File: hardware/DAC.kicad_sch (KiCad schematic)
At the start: 43 parts, among them J2 PJ-3270, U10 OPA1652, U11 LM4562, U9 WM8741

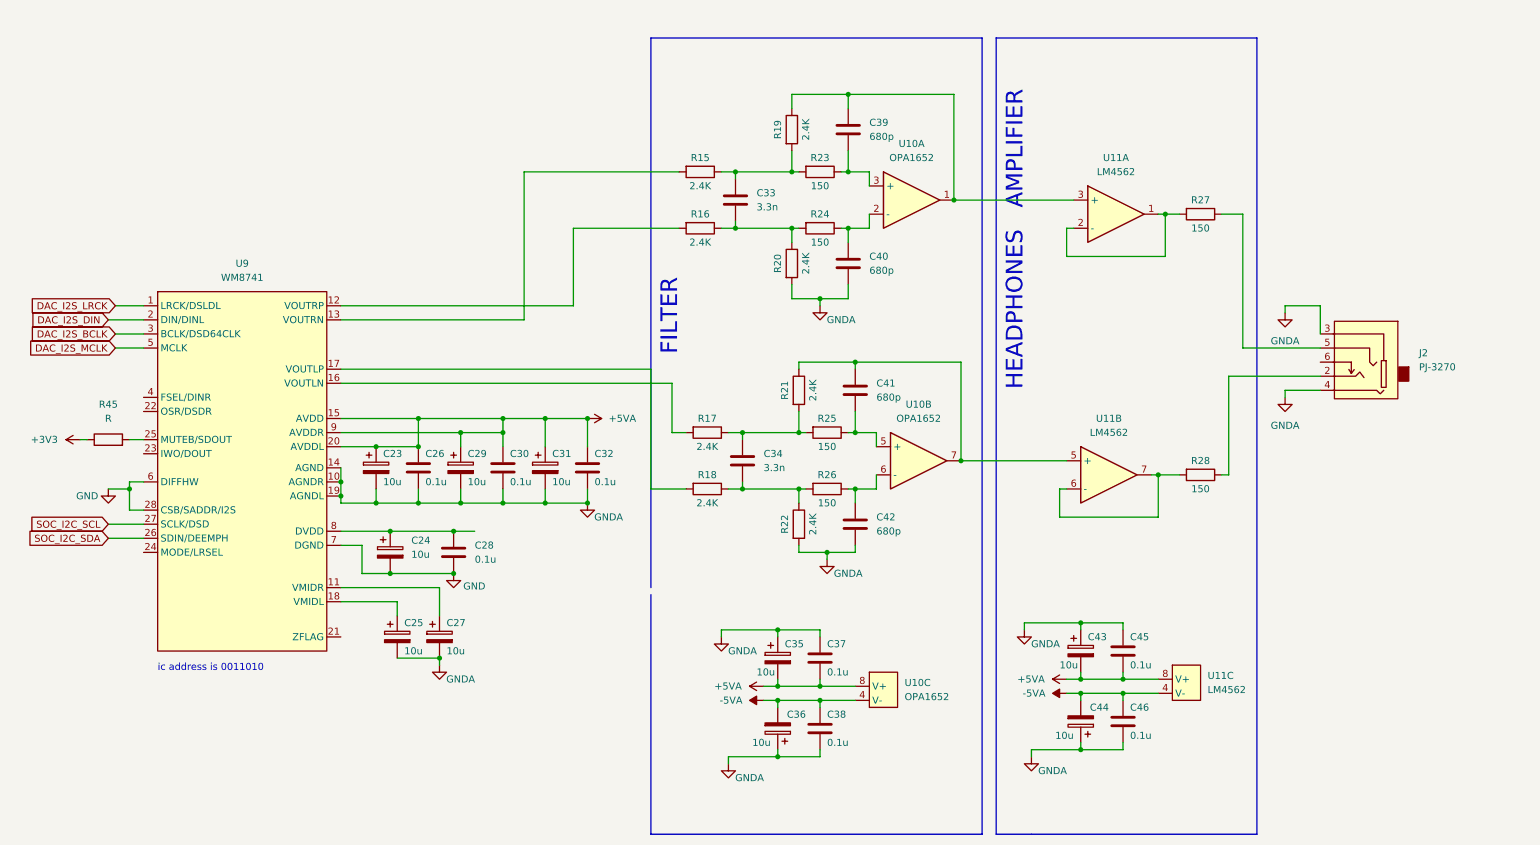
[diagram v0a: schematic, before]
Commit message: added hierarchy labels
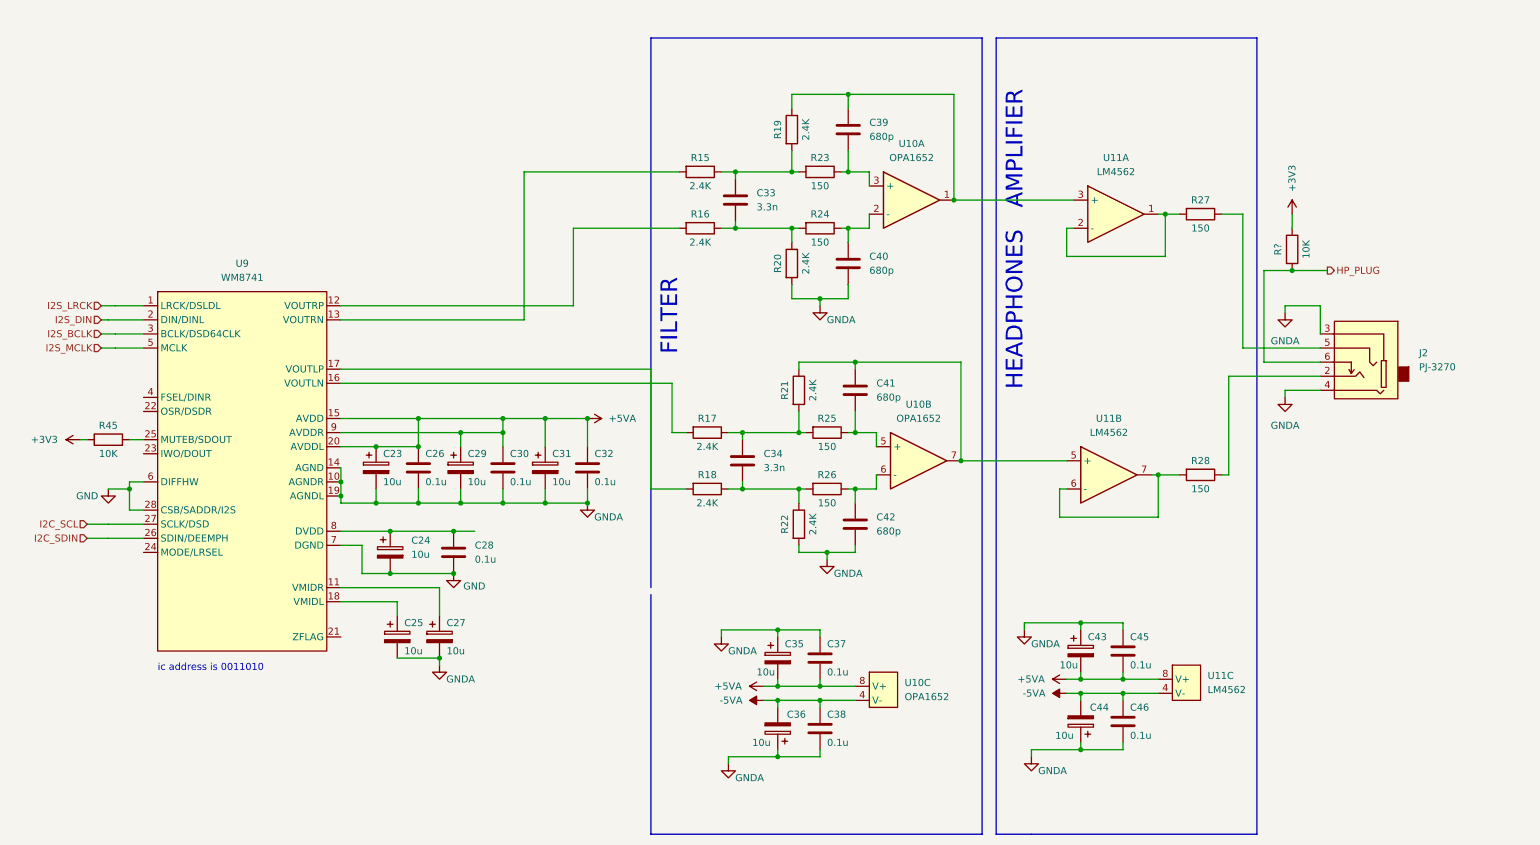
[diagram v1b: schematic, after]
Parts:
- added R?: 10K, symbol rlib_passive:R
- R45: value R -> 10K
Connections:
- net +3V3: now also R?.1
- net HP_PLUG: now reaches J2.6
- net HP_PLUG: now also R?.2
- net DAC_I2S_BCLK renamed I2S_BCLK
- net DAC_I2S_DIN renamed I2S_DIN
- net DAC_I2S_LRCK renamed I2S_LRCK
- net DAC_I2S_MCLK renamed I2S_MCLK
- net SOC_I2C_SCL renamed I2C_SCL
- net SOC_I2C_SDA renamed I2C_SDIN
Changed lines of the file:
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@@
   (junction (at 204.47 120.65) (diameter 0) (color 0 0 0 1)
   )
+  (junction (at 242.57 57.15) (diameter 0) (color 0 0 0 0)
+  )
   (junction (at 152.4 49.53) (diameter 0) (color 0 0 0 1)
   )
@@
     (stroke (width 0) (type default) (color 0 0 0 1))
   )
+  (wire (pts (xy 25.4 102.87) (xy 29.21 102.87))
+    (stroke (width 0) (type default) (color 0 0 0 0))
+  )
   (wire (pts (xy 163.83 96.52) (xy 167.64 96.52))
     (stroke (width 0) (type default) (color 0 0 0 1))
@@
     (stroke (width 0) (type default) (color 0 0 0 1))
   )
+  (wire (pts (xy 27.94 66.04) (xy 29.21 66.04))
+    (stroke (width 0) (type default) (color 0 0 0 0))
+  )
   (polyline (pts (xy 127 115.57) (xy 127 158.75))
     (stroke (width 0) (type default) (color 0 0 0 0))
@@
     (stroke (width 0) (type default) (color 0 0 0 1))
   )
+  (wire (pts (xy 242.57 57.15) (xy 248.92 57.15))
+    (stroke (width 0) (type default) (color 0 0 0 0))
+  )
   (wire (pts (xy 158.75 107.95) (xy 158.75 109.22))
     (stroke (width 0) (type default) (color 0 0 0 1))
@@
     (stroke (width 0) (type default) (color 0 0 0 1))
   )
+  (wire (pts (xy 247.65 73.66) (xy 237.49 73.66))
+    (stroke (width 0) (type default) (color 0 0 0 0))
+  )
   (wire (pts (xy 229.87 93.98) (xy 231.14 93.98))
     (stroke (width 0) (type default) (color 0 0 0 1))
@@
     (stroke (width 0) (type default) (color 0 0 0 1))
   )
+  (wire (pts (xy 242.57 57.15) (xy 237.49 57.15))
+    (stroke (width 0) (type default) (color 0 0 0 0))
+  )
   (wire (pts (xy 204.47 143.51) (xy 204.47 142.24))
     (stroke (width 0) (type default) (color 0 0 0 1))
@@
     (stroke (width 0) (type default) (color 0 0 0 1))
   )
+  (wire (pts (xy 27.94 71.12) (xy 30.48 71.12))
+    (stroke (width 0) (type default) (color 0 0 0 0))
+  )
   (wire (pts (xy 218.44 93.98) (xy 222.25 93.98))
     (stroke (width 0) (type default) (color 0 0 0 1))
@@
     (stroke (width 0) (type default) (color 0 0 0 1))
   )
+  (wire (pts (xy 27.94 63.5) (xy 30.48 63.5))
+    (stroke (width 0) (type default) (color 0 0 0 0))
+  )
+  (wire (pts (xy 237.49 73.66) (xy 237.49 57.15))
+    (stroke (width 0) (type default) (color 0 0 0 0))
+  )
   (wire (pts (xy 231.14 93.98) (xy 231.14 76.2))
     (stroke (width 0) (type default) (color 0 0 0 1))
@@
     (stroke (width 0) (type default) (color 0 0 0 1))
   )
+  (wire (pts (xy 242.57 46.99) (xy 242.57 49.53))
+    (stroke (width 0) (type default) (color 0 0 0 0))
+  )
   (wire (pts (xy 229.87 46.99) (xy 233.68 46.99))
     (stroke (width 0) (type default) (color 0 0 0 1))
@@
   (wire (pts (xy 201.93 130.81) (xy 204.47 130.81))
     (stroke (width 0) (type default) (color 0 0 0 1))
+  )
+  (wire (pts (xy 25.4 105.41) (xy 29.21 105.41))
+    (stroke (width 0) (type default) (color 0 0 0 0))
+  )
+  (wire (pts (xy 27.94 68.58) (xy 30.48 68.58))
+    (stroke (width 0) (type default) (color 0 0 0 0))
   )
   (wire (pts (xy 219.71 46.99) (xy 218.44 46.99))
@@
     (effects (font (size 3 3)) (justify left bottom))
   )
-  (global_label "DAC_I2S_LRCK" (shape input) (at 30.48 63.5 180) (fields_autoplaced)
+  (hierarchical_label "I2S_LRCK" (shape input) (at 27.94 63.5 180)
     (effects (font (size 1.27 1.27)) (justify right))
-    (property "Intersheet References" "${INTERSHEET_REFS}" (id 0) (at 14.6412 63.4206 0)
-      (effects (font (size 1.27 1.27)) (justify right) hide)
-    )
-  )
-  (global_label "SOC_I2C_SDA" (shape input) (at 29.21 105.41 180) (fields_autoplaced)
+  )
+  (hierarchical_label "I2S_BCLK" (shape input) (at 27.94 68.58 180)
     (effects (font (size 1.27 1.27)) (justify right))
-    (property "Intersheet References" "${INTERSHEET_REFS}" (id 0) (at 14.3993 105.3306 0)
-      (effects (font (size 1.27 1.27)) (justify right) hide)
-    )
-  )
-  (global_label "DAC_I2S_DIN" (shape input) (at 29.21 66.04 180) (fields_autoplaced)
+  )
+  (hierarchical_label "I2S_MCLK" (shape input) (at 27.94 71.12 180)
     (effects (font (size 1.27 1.27)) (justify right))
-    (property "Intersheet References" "${INTERSHEET_REFS}" (id 0) (at 15.004 65.9606 0)
-      (effects (font (size 1.27 1.27)) (justify right) hide)
-    )
-  )
-  (global_label "DAC_I2S_MCLK" (shape input) (at 30.48 71.12 180) (fields_autoplaced)
+  )
+  (hierarchical_label "I2C_SCL" (shape input) (at 25.4 102.87 180)
     (effects (font (size 1.27 1.27)) (justify right))
-    (property "Intersheet References" "${INTERSHEET_REFS}" (id 0) (at 14.4598 71.0406 0)
-      (effects (font (size 1.27 1.27)) (justify right) hide)
-    )
-  )
-  (global_label "DAC_I2S_BCLK" (shape input) (at 30.48 68.58 180) (fields_autoplaced)
+  )
+  (hierarchical_label "I2S_DIN" (shape input) (at 27.94 66.04 180)
     (effects (font (size 1.27 1.27)) (justify right))
-    (property "Intersheet References" "${INTERSHEET_REFS}" (id 0) (at 14.6412 68.5006 0)
-      (effects (font (size 1.27 1.27)) (justify right) hide)
-    )
-  )
-  (global_label "SOC_I2C_SCL" (shape input) (at 29.21 102.87 180) (fields_autoplaced)
+  )
+  (hierarchical_label "I2C_SDIN" (shape input) (at 25.4 105.41 180)
     (effects (font (size 1.27 1.27)) (justify right))
-    (property "Intersheet References" "${INTERSHEET_REFS}" (id 0) (at 14.4598 102.7906 0)
-      (effects (font (size 1.27 1.27)) (justify right) hide)
-    )
+  )
+  (hierarchical_label "HP_PLUG" (shape output) (at 248.92 57.15 0)
+    (effects (font (size 1.27 1.27)) (justify left))
   )
   (symbol (lib_id "rlib_passive:C_Pol") (at 77.47 92.71 0) (unit 1)
@@
     (pin "1")
     (pin "2")
+  )
+  (symbol (lib_id "power:+3V3") (at 242.57 46.99 0) (unit 1)
+    (in_bom yes) (on_board yes)
+    (property "Reference" "#PWR?" (id 0) (at 242.57 50.8 0)
+      (effects (font (size 1.27 1.27)) hide)
+    )
+    (property "Value" "+3V3" (id 1) (at 242.57 38.1 90)
+      (effects (font (size 1.27 1.27)) (justify right))
+    )
+    (property "Footprint" "" (id 2) (at 242.57 46.99 0)
+      (effects (font (size 1.27 1.27)) hide)
+    )
+    (property "Datasheet" "" (id 3) (at 242.57 46.99 0)
+      (effects (font (size 1.27 1.27)) hide)
+    )
+    (pin "1")
   )
   (symbol (lib_id "rlib_passive:R") (at 137.16 86.36 270) (unit 1)
@@
   )
   (symbol (lib_id "rlib_passive:R") (at 29.21 87.63 90) (unit 1)
-    (in_bom yes) (on_board yes) (fields_autoplaced)
-    (property "Reference" "R45" (id 0) (at 29.21 81.28 90))
-    (property "Value" "R" (id 1) (at 29.21 83.82 90))
+    (in_bom yes) (on_board yes)
+    (property "Reference" "R45" (id 0) (at 29.21 85.09 90))
+    (property "Value" "10K" (id 1) (at 29.21 90.17 90))
     (property "Footprint" "rlib_passive:R_0603_1608Metric" (id 2) (at 29.21 89.408 90)
       (effects (font (size 1.27 1.27)) hide)
@@
     (pin "1")
     (pin "2")
+  )
+  (symbol (lib_id "rlib_passive:R") (at 242.57 53.34 0) (unit 1)
+    (in_bom yes) (on_board yes)
+    (property "Reference" "R?" (id 0) (at 240.03 53.34 90))
+    (property "Value" "10K" (id 1) (at 245.11 53.34 90))
+    (property "Footprint" "" (id 2) (at 240.792 53.34 90)
+      (effects (font (size 1.27 1.27)) hide)
+    )
+    (property "Datasheet" "~" (id 3) (at 242.57 53.34 0)
+      (effects (font (size 1.27 1.27)) hide)
+    )
+    (property "Tolerance" "" (id 4) (at 242.57 53.34 0))
+    (property "LSCS Partnumber" "" (id 5) (at 242.57 53.34 0))
+    (property "Manufacturer" "" (id 6) (at 242.57 53.34 0))
+    (pin "1")
+    (pin "2")

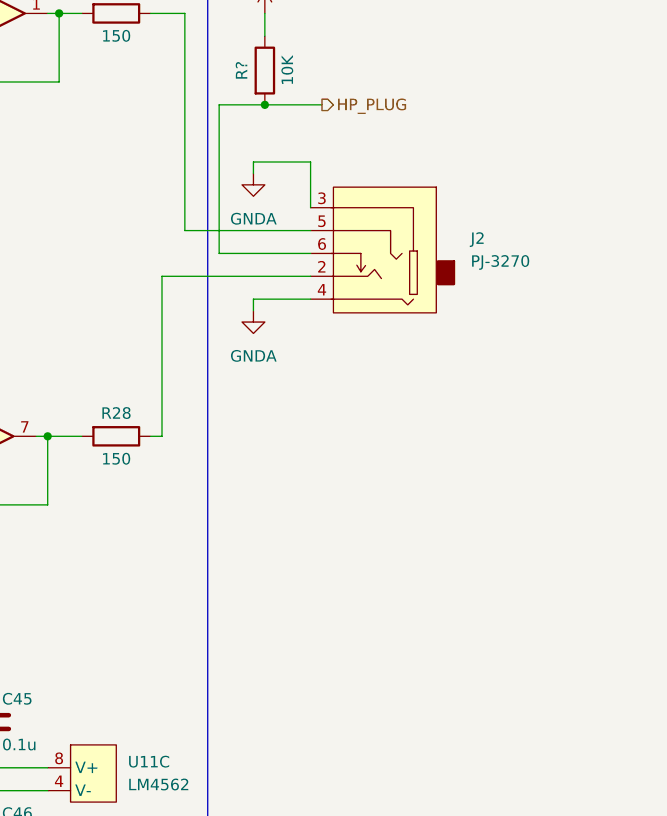
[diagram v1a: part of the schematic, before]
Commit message: added esd protection
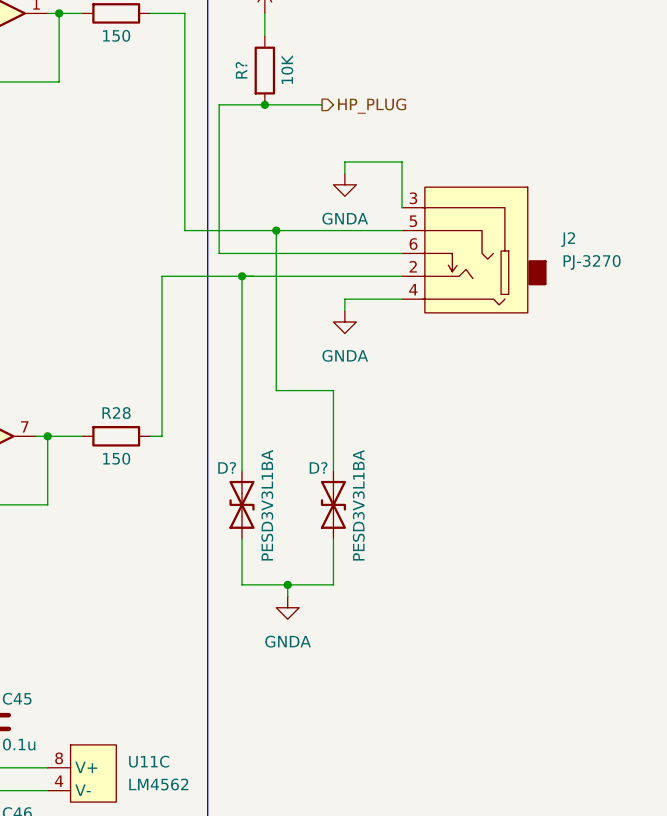
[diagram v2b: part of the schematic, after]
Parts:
- added D? (x2): PESD3V3L1BA, rlib_passive:D_SOD-323F, symbol rlib_passive:PESD3V3L1BA
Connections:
- net GNDA: now also D?.1 (A1), D?.1 (A1)
- net at J2.5, R27.1: now also D?.2 (A2)
- net at J2.2, R28.1: now also D?.2 (A2)
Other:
- moved on the sheet: J2

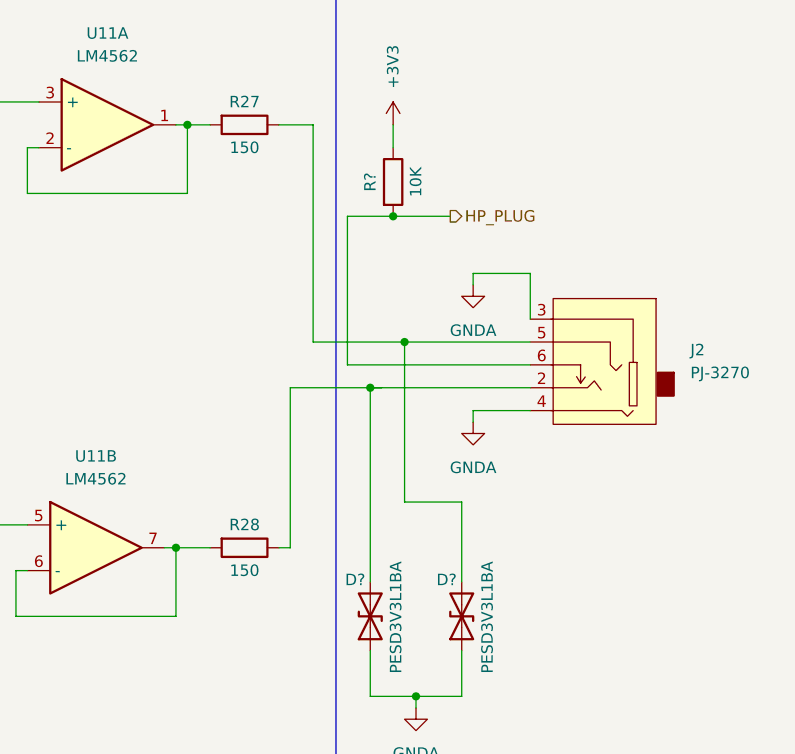
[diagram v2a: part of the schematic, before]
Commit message: replaced dc-dc ics
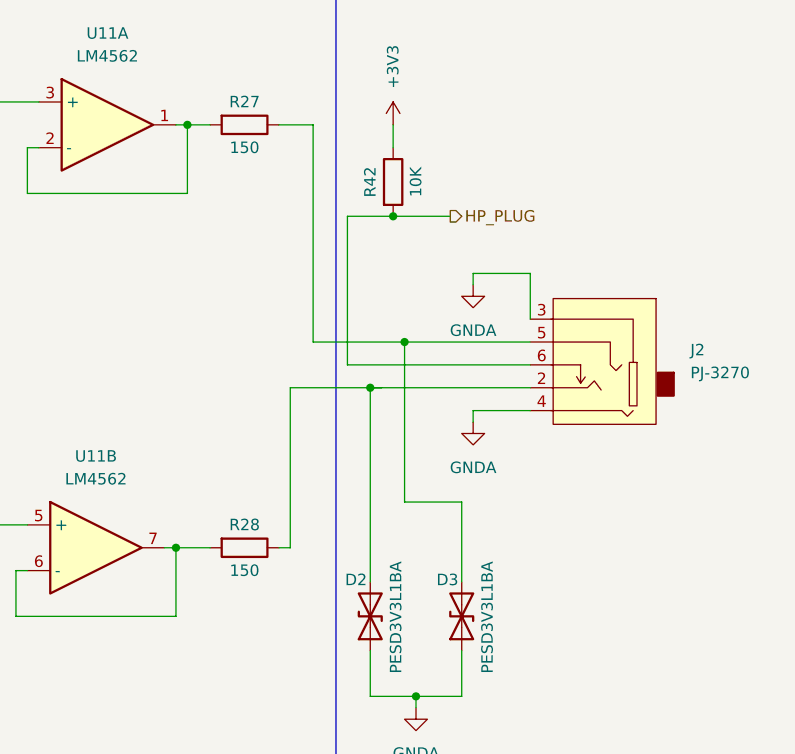
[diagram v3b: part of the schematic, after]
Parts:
- gave numbers to parts that had none: 3
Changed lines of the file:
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@@
   (symbol (lib_id "power:GNDA") (at 245.11 111.76 0) (unit 1)
     (in_bom yes) (on_board yes)
-    (property "Reference" "#PWR?" (id 0) (at 245.11 118.11 0)
+    (property "Reference" "#PWR0199" (id 0) (at 245.11 118.11 0)
       (effects (font (size 1.27 1.27)) hide)
     )
@@
   (symbol (lib_id "power:+3V3") (at 242.57 46.99 0) (unit 1)
     (in_bom yes) (on_board yes)
-    (property "Reference" "#PWR?" (id 0) (at 242.57 50.8 0)
+    (property "Reference" "#PWR0155" (id 0) (at 242.57 50.8 0)
       (effects (font (size 1.27 1.27)) hide)
     )
@@
   (symbol (lib_id "rlib_passive:PESD3V3L1BA") (at 240.03 101.6 90) (unit 1)
     (in_bom yes) (on_board yes)
-    (property "Reference" "D?" (id 0) (at 237.2203 97.5472 90)
+    (property "Reference" "D2" (id 0) (at 237.2203 97.5472 90)
       (effects (font (size 1.27 1.27)) (justify right))
     )
@@
   (symbol (lib_id "rlib_passive:PESD3V3L1BA") (at 250.19 101.6 90) (unit 1)
     (in_bom yes) (on_board yes)
-    (property "Reference" "D?" (id 0) (at 247.3803 97.5472 90)
+    (property "Reference" "D3" (id 0) (at 247.3803 97.5472 90)
       (effects (font (size 1.27 1.27)) (justify right))
     )
@@
   (symbol (lib_id "rlib_passive:R") (at 242.57 53.34 0) (unit 1)
     (in_bom yes) (on_board yes)
-    (property "Reference" "R?" (id 0) (at 240.03 53.34 90))
+    (property "Reference" "R42" (id 0) (at 240.03 53.34 90))
     (property "Value" "10K" (id 1) (at 245.11 53.34 90))
     (property "Footprint" "" (id 2) (at 240.792 53.34 90)
